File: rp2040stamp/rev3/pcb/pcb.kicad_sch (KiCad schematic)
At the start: 26 parts, among them U1 RP2040, U2 Memory_Flash_W25Q64_XSON, U3 NCP114ASN330T1G, X1 12.000MHz

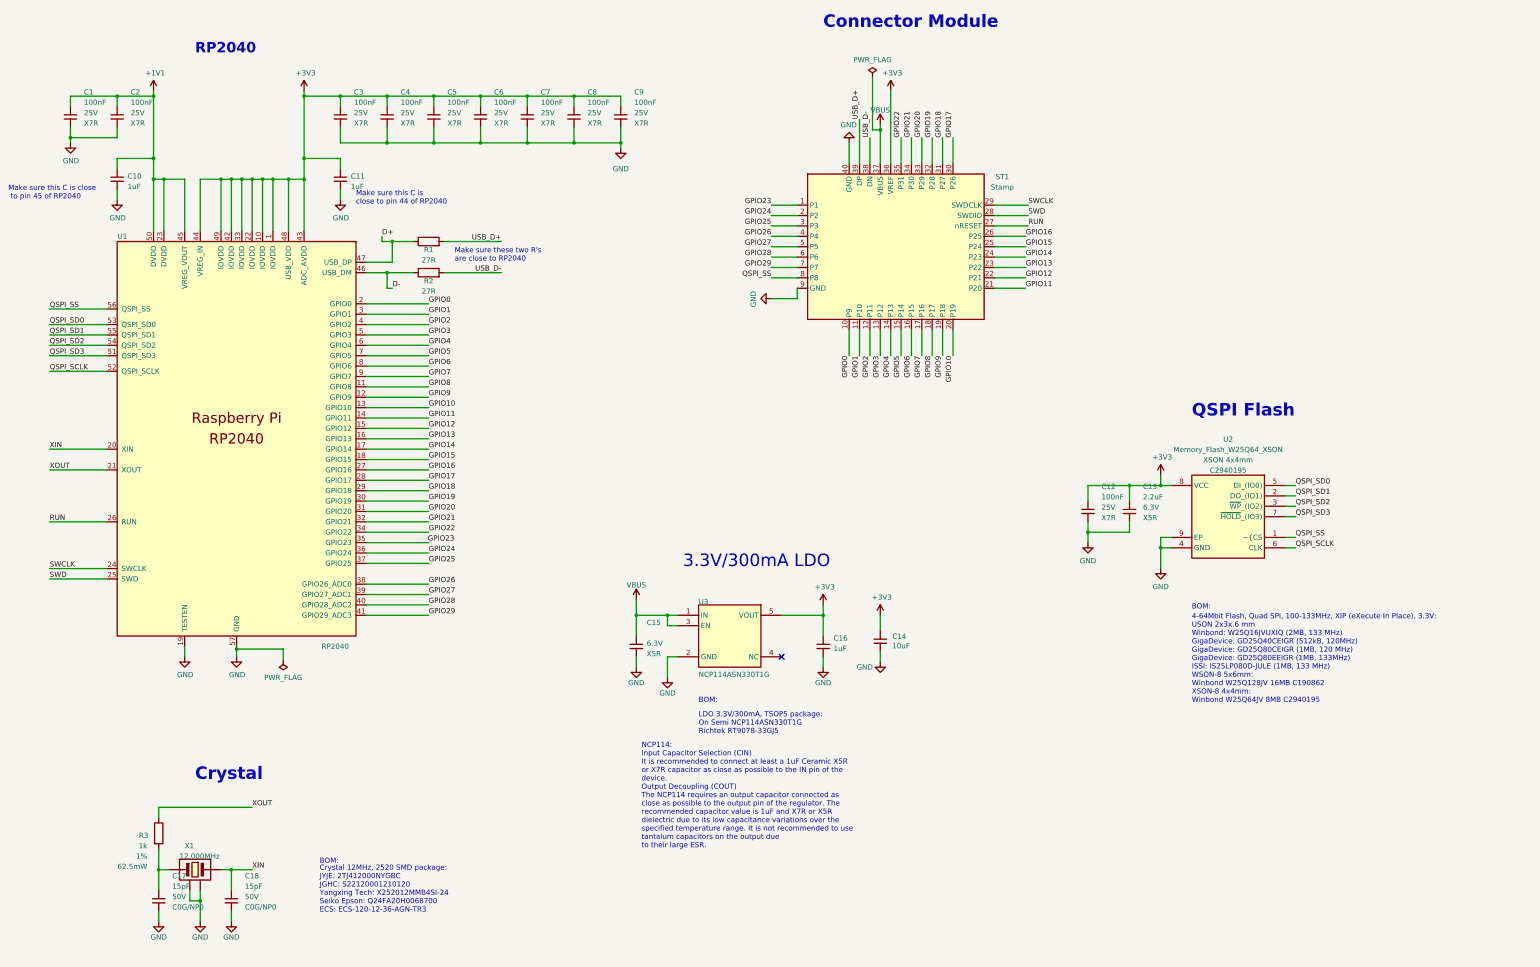
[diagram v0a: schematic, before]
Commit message: M  giri-kicad-lib/switches_lib.pretty/Gateron_1.25u_v2.kicad_mod M  giri-kicad-lib/switches_lib.pretty/Gateron_1u_v2.kicad_mod M  giri-kicad-lib/switches_lib.pretty/Gateron_2u_v2.kicad_mod A  giri-kicad-lib/switches_lib.pretty/SMTSO_M2_FrontPad_M2_hole.kicad_mod A  giri-kicad-lib/switches_lib.pretty/Switch_Cutout2_MX.kicad_mod A  giri-kicad-lib/switches_lib.pretty/Switch_Cutout2_MX_1.25u.kicad_mod A  giri-kicad-lib/switches_lib.pretty/Switch_Cutout2_MX_2u.kicad_mod M  mx/rev3/bottom-cover/pcb/pcb.kicad_pcb M  mx/rev3/bottom-cover/pcb/pcb.kicad_prl M  mx/rev3/bottom-cover/pcb/pcb.kicad_sch M  mx/rev3/pcb-rev2/pcb/pcb.kicad_pcb M  mx/rev3/pcb-rev2/pcb/pcb.kicad_prl M  mx/rev3/pcb-rev2/pcb/pcb.kicad_sch M  mx/rev3/switch-plate-wide/fp-lib-table M  mx/rev3/switch-plate-wide/switch-plate-wide.kicad_pcb M  mx/rev3/switch-plate-wide/switch-plate-wide.kicad_sch A  mx/rev4/notes D  nrfStamp/rev1/pcb/~pcb.kicad_sch.lck D  rp2040stamp/rev2/pcb/~pcb.kicad_sch.lck M  rp2040stamp/rev3/pcb/fp-lib-table M  rp2040stamp/rev3/pcb/pcb.kicad_pcb M  rp2040stamp/rev3/pcb/pcb.kicad_prl M  rp2040stamp/rev3/pcb/pcb.kicad_sch M  rp2040stamp/rev3/pcb/sym-lib-table
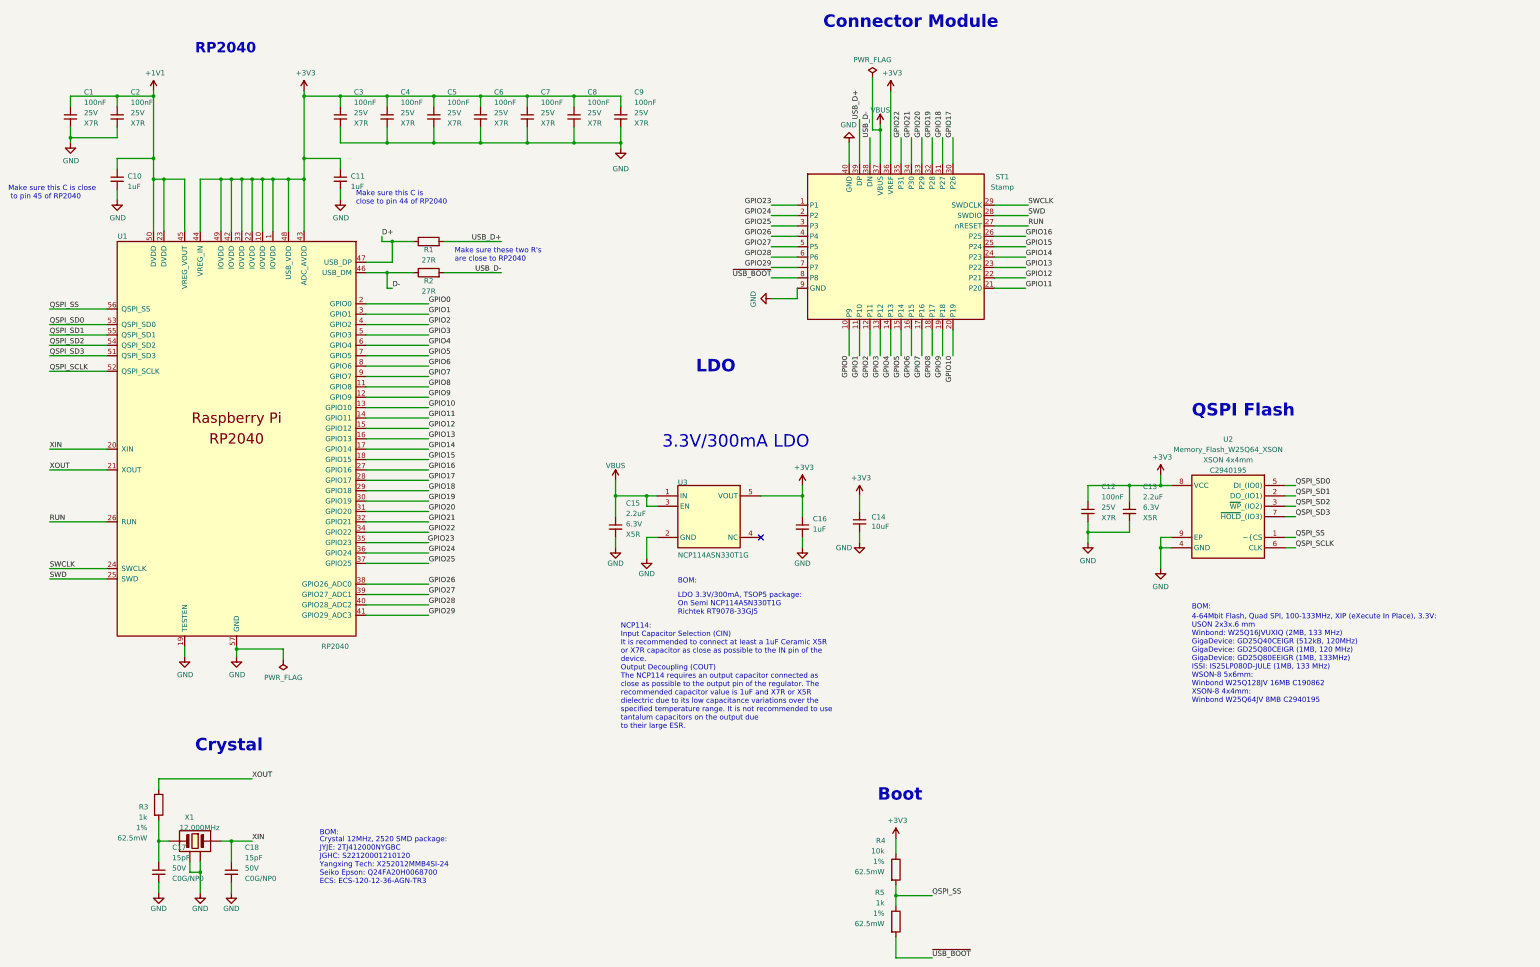
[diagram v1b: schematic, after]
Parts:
- added R4: 10k, RP2040_Minimal:R_0603_1608Metric_Pad0.98x0.95mm_HandSolder, symbol Device:R
- added R5: 1k, RP2040_Minimal:R_0603_1608Metric_Pad0.98x0.95mm_HandSolder, symbol Device:R
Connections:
- net +3V3: now also R4.1
- net QSPI_SS: now also R4.2, R5.1; no longer ST1.8 (P8)
- new net ~{USB_BOOT}: R5.2, ST1.8 (P8)
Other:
- note added: "Boot"
- note added: "LDO"
- moved on the sheet: C14, C15, C16, C17, C18, R3, U3, X1
